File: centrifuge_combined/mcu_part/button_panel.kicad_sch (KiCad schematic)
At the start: 5 parts, among them U507 4x4_keyboard

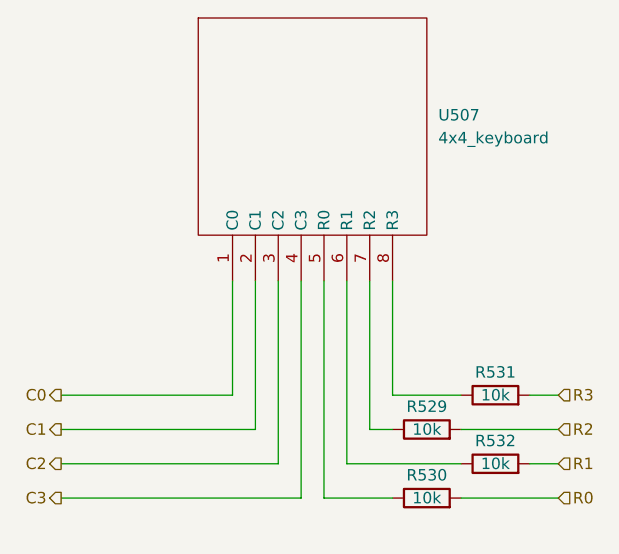
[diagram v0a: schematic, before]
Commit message: change resistor values to have to 2k2, and also make I2C hopefully work
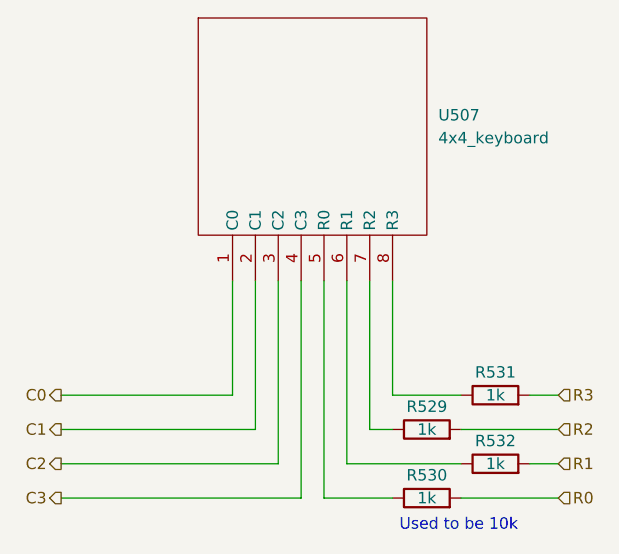
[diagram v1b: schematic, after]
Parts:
- R529, R530, R531, R532: value 10k -> 1k
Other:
- note added: "Used to be 10k"
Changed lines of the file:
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@@
     (stroke (width 0) (type default) (color 0 0 0 0))
+  )
+  (text "Used to be 10k" (at 163.322 129.54 0)
+    (effects (font (size 1.27 1.27)) (justify left bottom))
   )
   (hierarchical_label "C1" (shape output) (at 125.73 118.11 180)
@@
     (in_bom yes) (on_board yes)
     (property "Reference" "R529" (id 0) (at 166.37 115.57 90))
-    (property "Value" "10k" (id 1) (at 166.37 118.11 90))
+    (property "Value" "1k" (id 1) (at 166.37 118.11 90))
     (property "Footprint" "Resistor_SMD:R_0805_2012Metric_Pad1.20x1.40mm_HandSolder" (id 2) (at 166.37 119.888 90)
       (effects (font (size 1.27 1.27)) hide)
@@
     (in_bom yes) (on_board yes)
     (property "Reference" "R531" (id 0) (at 173.99 111.76 90))
-    (property "Value" "10k" (id 1) (at 173.99 114.3 90))
+    (property "Value" "1k" (id 1) (at 173.99 114.3 90))
     (property "Footprint" "Resistor_SMD:R_0805_2012Metric_Pad1.20x1.40mm_HandSolder" (id 2) (at 173.99 116.078 90)
       (effects (font (size 1.27 1.27)) hide)
@@
     (in_bom yes) (on_board yes)
     (property "Reference" "R532" (id 0) (at 173.99 119.38 90))
-    (property "Value" "10k" (id 1) (at 173.99 121.92 90))
+    (property "Value" "1k" (id 1) (at 173.99 121.92 90))
     (property "Footprint" "Resistor_SMD:R_0805_2012Metric_Pad1.20x1.40mm_HandSolder" (id 2) (at 173.99 123.698 90)
       (effects (font (size 1.27 1.27)) hide)
@@
     (in_bom yes) (on_board yes)
     (property "Reference" "R530" (id 0) (at 166.37 123.19 90))
-    (property "Value" "10k" (id 1) (at 166.37 125.73 90))
+    (property "Value" "1k" (id 1) (at 166.37 125.73 90))
     (property "Footprint" "Resistor_SMD:R_0805_2012Metric_Pad1.20x1.40mm_HandSolder" (id 2) (at 166.37 127.508 90)
       (effects (font (size 1.27 1.27)) hide)
